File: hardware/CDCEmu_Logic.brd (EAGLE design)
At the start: 60 x 40 mm, 28 parts, among them J1 CAN, J2 ICSP, Q1 BC546A, U1 7805, U2 ATTINY85, U3 MCP2515, U4 1050, U5 PCF8574P, Y1 8MHz

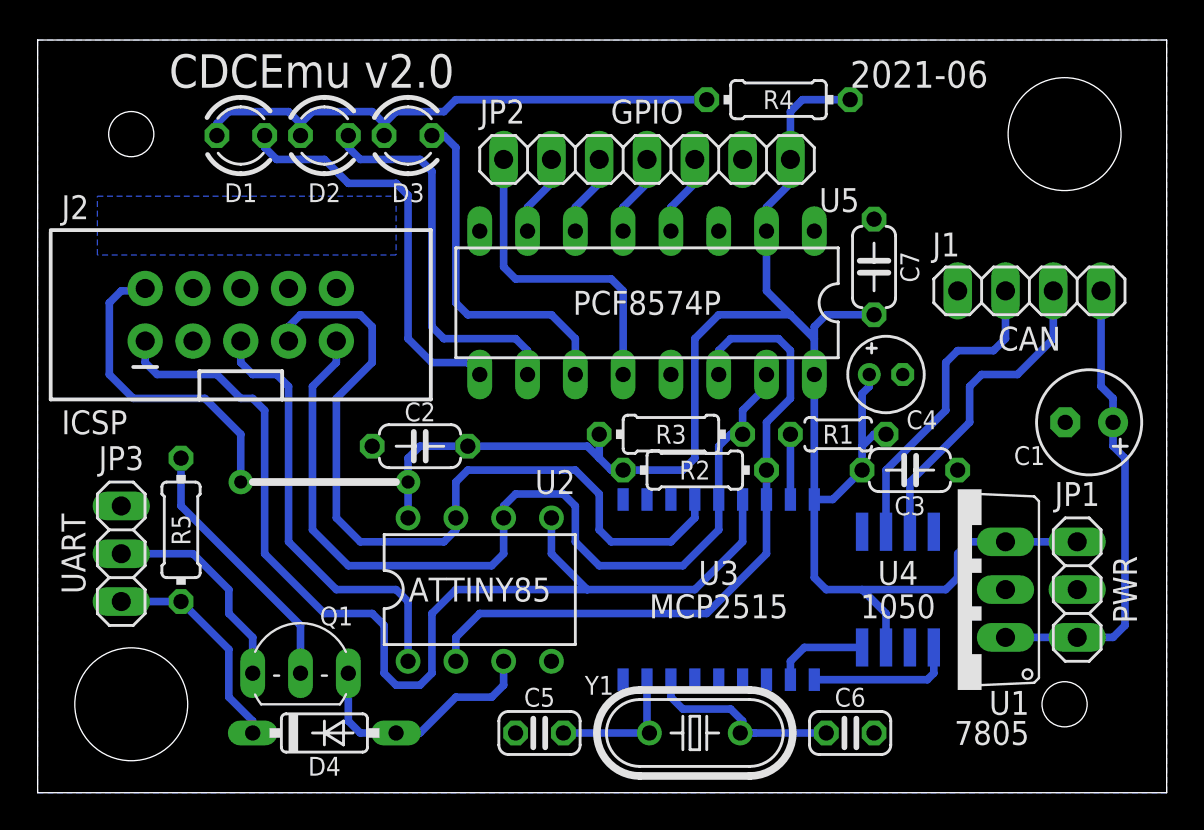
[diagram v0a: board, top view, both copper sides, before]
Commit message: [HW] Refactor logic PCB
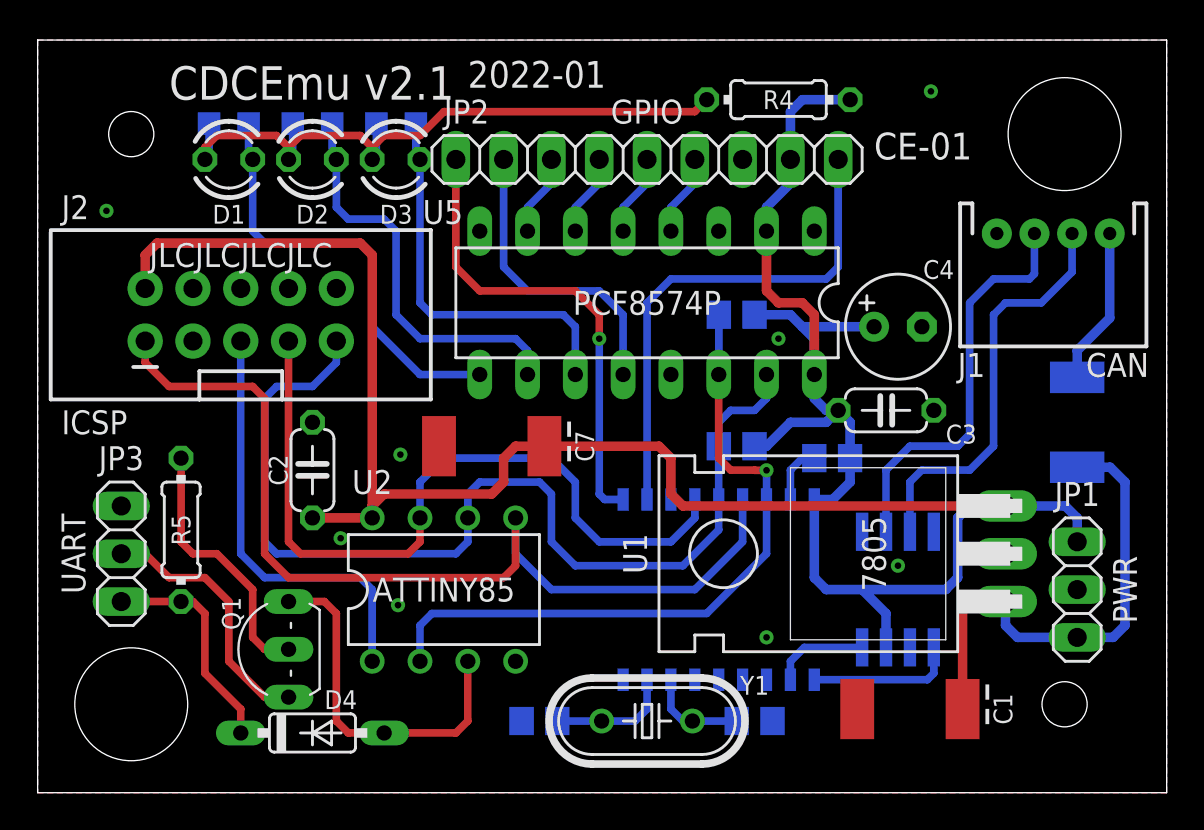
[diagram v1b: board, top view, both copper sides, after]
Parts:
- added D5, D6, D7: (no value), led:CHIP-LED0805
- added F1: 500mA, SparkFun-Fuses:1812
- C1: value 100u -> 10u; device rcl:E2,5-6 -> custom:C2512-POL
- C4: device rcl:E1,8-4 -> rcl:E2,5-6
- C5, C6: device rcl:C025-024X044 -> rcl:C0805
- C7: value 100n -> 47u; device rcl:C050-024X044 -> custom:C2512-POL
- J1: device pinhead:1X04 -> SparkFun-Connectors:JST-4-PTH
- JP2: device pinhead:1X07 -> pinhead:1X09
- R1: device rcl:0204/5 -> rcl:R0805
- R2, R3: value 2k2 -> 2.2k; device rcl:0204/7 -> rcl:R0805
- U1: device linear:TO220V -> custom:TO220H-NOHOLE
- moved C7 22.4 mm to (24.1, 18.4), turned to 180 degrees
- moved C1 18.0 mm to (46.4, 4.45)
- moved R2 8.55 mm to (37.1, 25.4), flipped to the bottom
- moved U1 7.85 mm to (41.3, 12.7)
- moved C2 5.85 mm to (14.6, 17.1), turned to 90 degrees
- moved C6 5.12 mm to (38.1, 3.81), flipped to the bottom, turned to 180 degrees
- moved R3 3.55 mm to (37.1, 18.4), flipped to the bottom
- moved C3 3.42 mm to (45.1, 20.3)
- moved J1 3.30 mm to (54.0, 29.7)
- moved Y1 2.62 mm to (32.4, 3.81)
- moved C4 2.62 mm to (45.7, 24.8)
- moved Q1 1.91 mm to (12.1, 7.62), turned to 90 degrees
- moved U2 1.91 mm to (21.6, 10.8)
- moved D1 1.42 mm to (10.2, 33.7)
- moved D2 1.42 mm to (14.6, 33.7)
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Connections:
- new net G0: JP2.1, U3.11
- new net G1: JP2.9, U3.10
- new net VIN: F1.1, J1.1
- net +12V: now also F1.2; no longer J1.1
- net +5V: now also C7.+, JP2.2; no longer C7.1, JP2.1
- net GND: now also C7.-, JP2.3; no longer C7.2, JP2.2
- net LED_A: now also D5.A, D6.A, D7.A
- net P0: now also JP2.4; no longer JP2.3
- net P1: now also JP2.5; no longer JP2.4
- net P2: now also JP2.6; no longer JP2.5
- net P3: now also JP2.7; no longer JP2.6
- net P4: now also D5.C
- net P5: now also D6.C
- net P6: now also D7.C
- net P7: now also JP2.8; no longer JP2.7
- net RX: now also D4.C, JP3.3, R5.1; no longer JP3.2, Q1.C
- net TX: now also JP3.2, Q1.C; no longer D4.C, JP3.3, R5.1
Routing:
- net G0: track 0.00 -> 27.1 mm
- net G1: track 0.00 -> 25.3 mm, vias 0 -> 1
- net +5V: track 121.9 -> 141.4 mm, vias 2 -> 0
- net VIN: track 0.00 -> 8.36 mm
- net LED_A: track 29.5 -> 36.7 mm
- net PB0: track 57.8 -> 51.3 mm
- net PB1: track 49.2 -> 55.0 mm
- net PB4: track 13.4 -> 19.2 mm
- net CANL: track 16.5 -> 21.7 mm
- net CANOSC2: track 10.5 -> 5.32 mm
- net CANH: track 17.1 -> 22.0 mm
- net PB2: track 43.5 -> 40.9 mm
- net TX: track 11.7 -> 13.9 mm
- net P6: track 18.8 -> 20.9 mm
- net P4: track 21.5 -> 23.3 mm
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- added copper zone on layer 1, net GND
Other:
- board text added: "2022-01"
- board text added: "CDCEmu v2.1"
- board text added: "CE-01"
- board text added: "GPIO"
- board text added: "JLCJLCJLCJLC"
- board text added: "JP1"
- board text added: "JP2"
- board text added: "JP3"
- board text added: "PWR"
- board text added: "UART"
- board text added: "https://github.com/kuba2k2/CDCEmu"
- board text added: "© kuba2k2"
- board text removed: "2021-06"
- board text removed: "CDCEmu v2.0"
